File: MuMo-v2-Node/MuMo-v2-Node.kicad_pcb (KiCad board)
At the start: 2 copper layers, 52.1 x 50 mm, 76 parts, among them Q1 Si1308EDL, SW1 Boot0, SW2 Reset, U1 MCP73123, U2 LoRa-E5, U3 CP2102N, U4 eInk_Display_1.54"200x200px, U5 BME680, U6 TSL25911, U7 BR24G512FVT-5AE2

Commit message: cleaned datasheets
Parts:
- removed the D1 at (146.1, 75.2)
- added D4: SP0503BAHTG, thisProjectLibrary:SP0503BAHTG-SOT143, F.Cu at (146.1, 75.2)
- R1: value 3K -> 3K3
- moved U4 3.60 mm to (152.6, 68.5)
- moved R6 0.43 mm to (183.6, 69.7)
- moved TP2 0.31 mm to (186.5, 67.3)
- moved TP3 0.30 mm to (186.5, 69.8)
- moved F2 0.05 mm to (145.5, 100.8)
- turned TP4 to -90 degrees
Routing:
- net GND: vias 24 -> 33

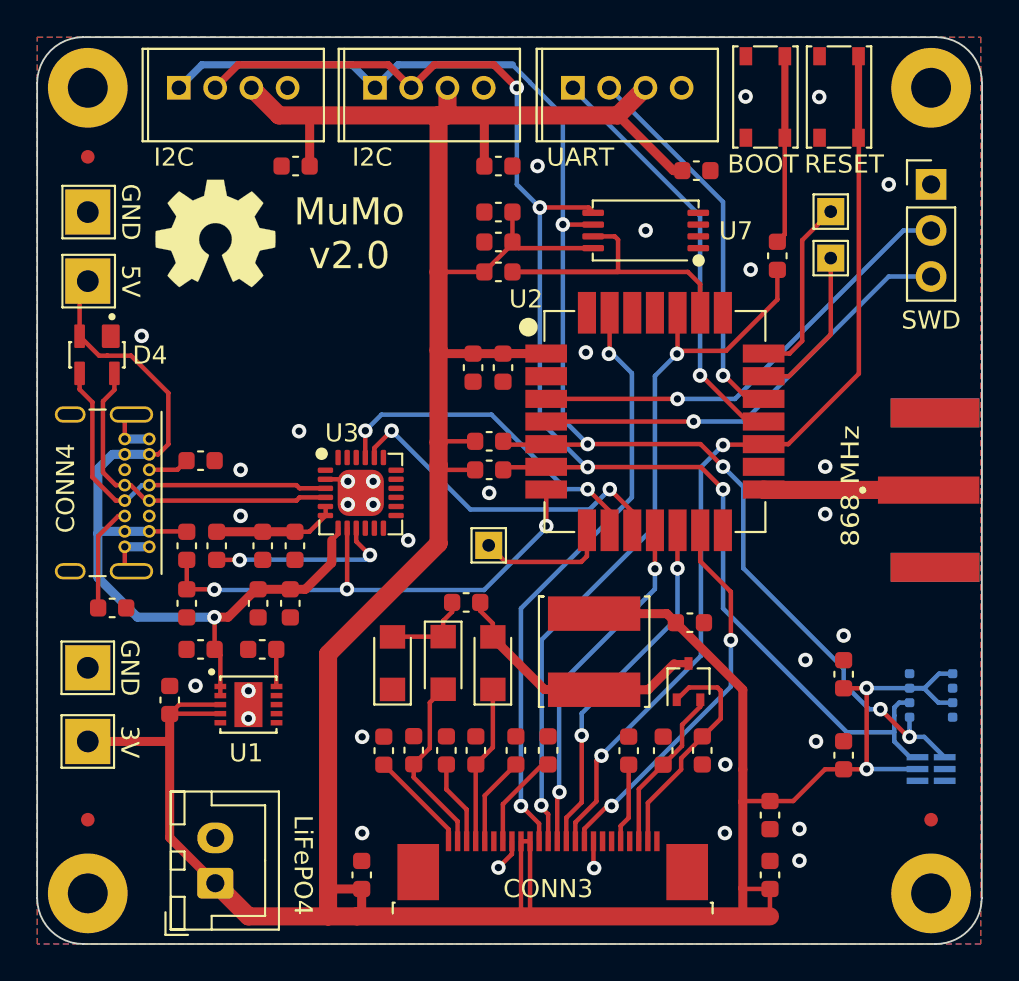
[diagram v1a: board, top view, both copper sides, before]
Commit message: added GND vias
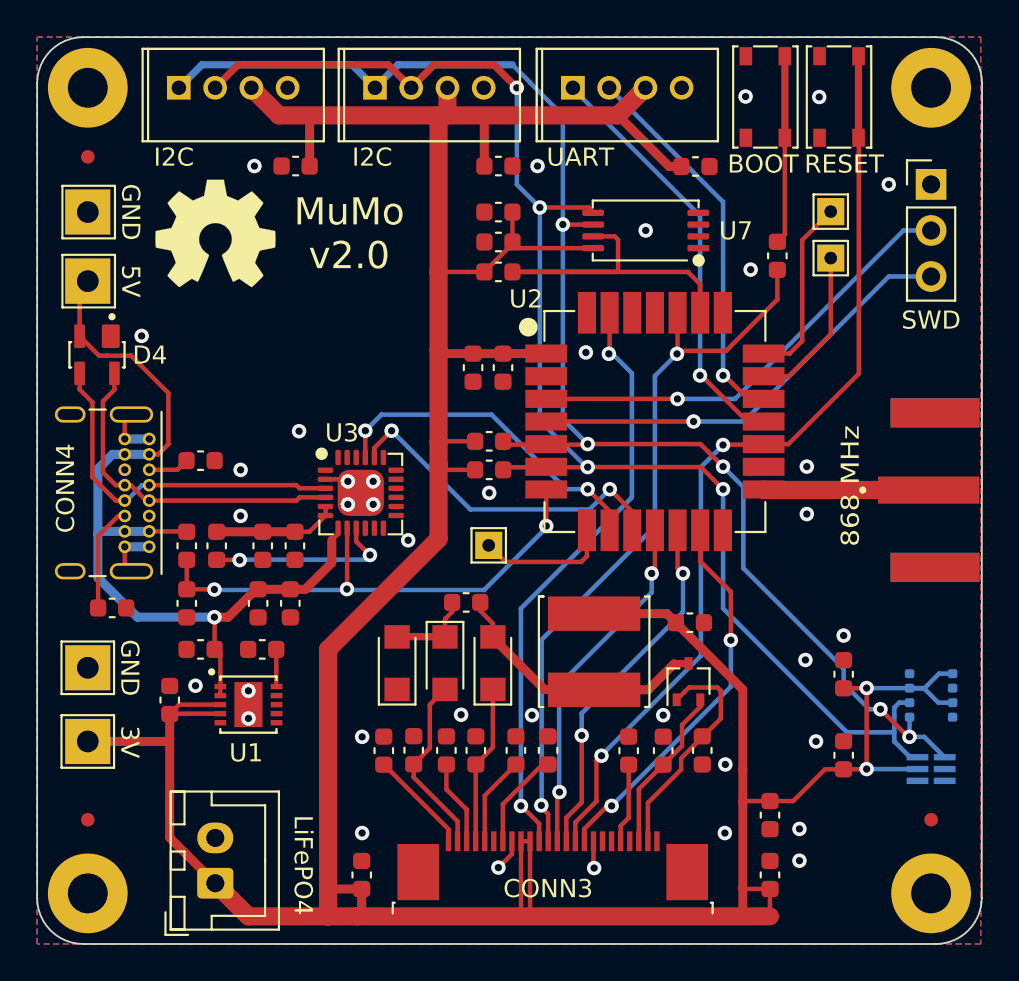
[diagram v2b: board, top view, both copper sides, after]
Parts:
- moved D1 0.25 mm to (162.6, 92.2)
- moved C17 0.23 mm to (179.1, 64.8)
- moved D2 0.10 mm to (165.3, 92.2)
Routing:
- net GND: vias 33 -> 37
